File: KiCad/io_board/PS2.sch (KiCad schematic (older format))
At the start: 1 part

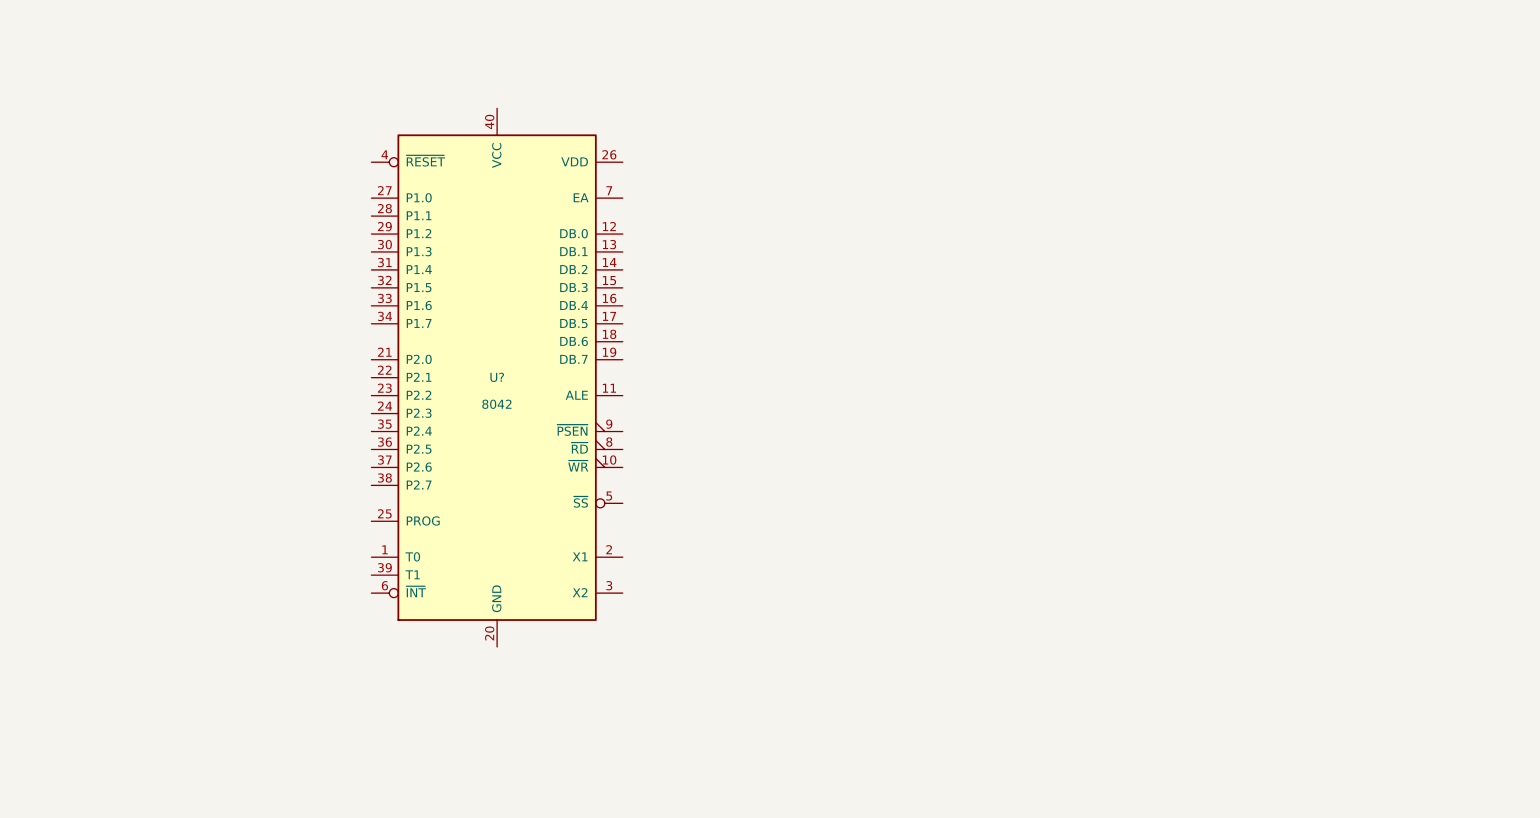
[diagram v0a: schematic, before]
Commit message: Updated IO board schematics and board.
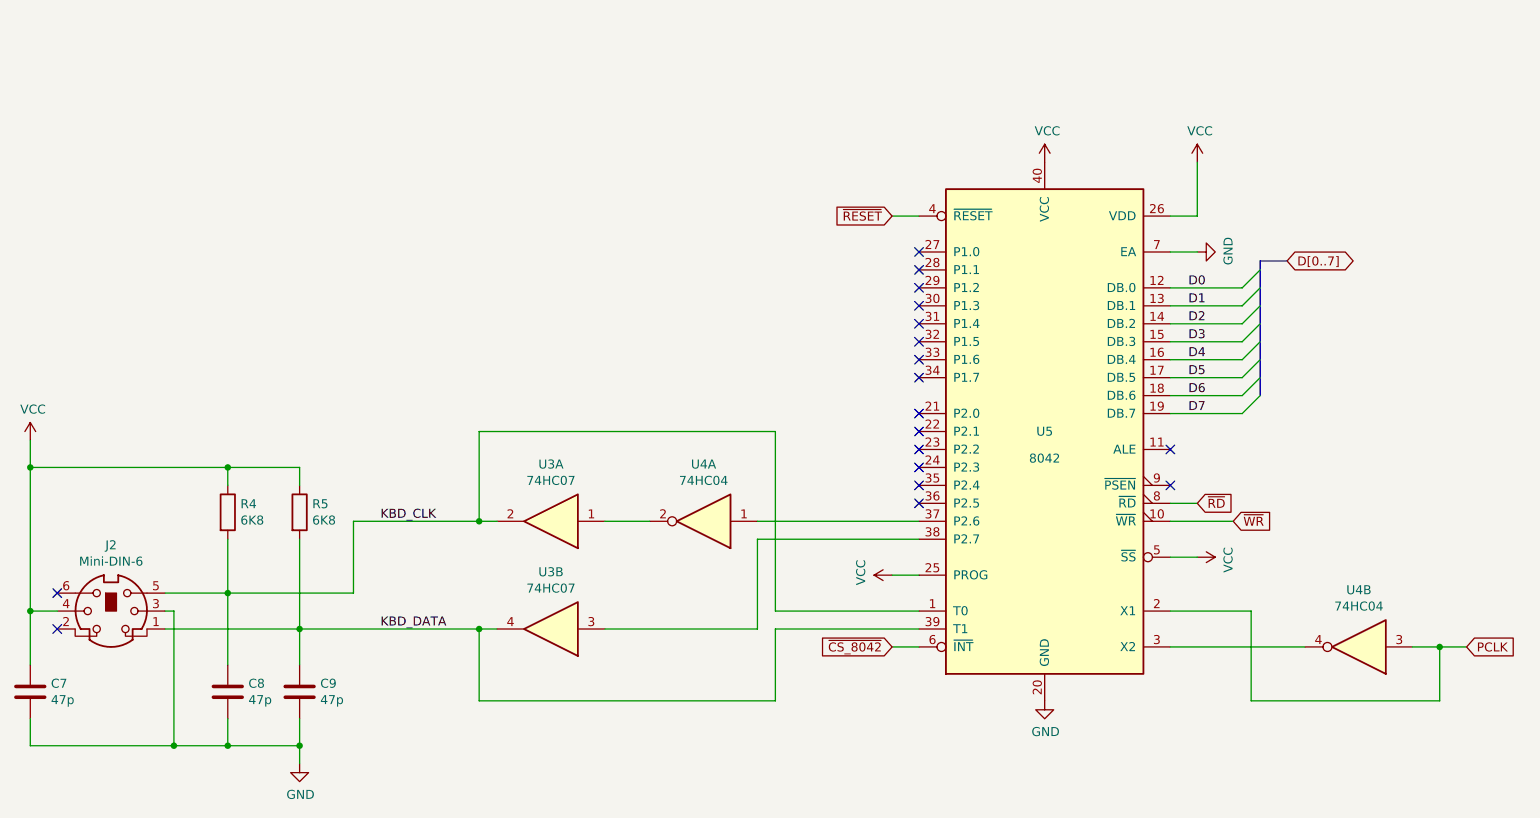
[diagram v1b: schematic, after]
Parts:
- added C7, C8, C9: 47p, Capacitor_THT:C_Disc_D3.0mm_W1.6mm_P2.50mm, symbol Device:C
- added J2: Mini-DIN-6, Mini8086:Mini_din6, symbol Connector:Mini-DIN-6
- added R4, R5: 6K8, Resistor_THT:R_Axial_DIN0207_L6.3mm_D2.5mm_P7.62mm_Horizontal, symbol Device:R
- added U3: 74HC07, Package_DIP:DIP-14_W7.62mm_LongPads, symbol 74xx:SN74LS07N
- added U4: 74HC04, symbol 74xx:74HC04
- U5: renamed from U?; footprint (none) -> Package_DIP:DIP-40_W15.24mm_Socket_LongPads
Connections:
- net KBD_CLK: now reaches U5.1 (T0)
- net KBD_CLK: now also C8.1, J2.5, R4.2, U3.2
- net ~WR: now reaches U5.10 (~WR~)
- net D0: now reaches U5.12 (DB.0)
- net D1: now reaches U5.13 (DB.1)
- net D2: now reaches U5.14 (DB.2)
- net D3: now reaches U5.15 (DB.3)
- net D4: now reaches U5.16 (DB.4)
- net D5: now reaches U5.17 (DB.5)
- net D6: now reaches U5.18 (DB.6)
- net D7: now reaches U5.19 (DB.7)
- net PCLK: now reaches U5.2 (X1)
- net PCLK: now also U4.3
- net GND: now reaches U5.20 (GND)
- net GND: now also U5.7 (EA), C7.2, C8.2, C9.2, J2.3
- net VCC: now reaches U5.25 (PROG)
- net VCC: now also U5.26 (VDD), U5.40 (VCC), U5.5 (~SS~), C7.1, J2.4, R4.1, R5.1
- net at U5.3 (X2): now also U4.4
- net at U5.37 (P2.6): now also U4.1
- net at U5.38 (P2.7): now also U3.3
- net KBD_DATA: now reaches U5.39 (T1)
- net KBD_DATA: now also C9.1, J2.1, R5.2, U3.4
- net ~RESET: now reaches U5.4 (~RESET~)
- net ~CS_8042: now reaches U5.6 (~INT~)
- net ~RD: now reaches U5.8 (~RD~)
- new net: U3.1, U4.2
- no-connect marks 0 -> 18
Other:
- moved on the sheet: U5

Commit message: Worked on I/O board.
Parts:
- U4: footprint (none) -> Package_SO:SOIC-14_3.9x8.7mm_P1.27mm
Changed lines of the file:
@@
 encoding utf-8
 Sheet 3 7
-Title ""
-Date ""
+Title "Mini8086 I/O board"
+Date "2020-11-05"
 Rev "1.0"
 Comp ""
@@
 F 0 "U4" H 5550 3533 50  0000 C CNN
 F 1 "74HC04" H 5550 3624 50  0000 C CNN
-F 2 "" H 5550 3850 50  0001 C CNN
+F 2 "Package_SO:SOIC-14_3.9x8.7mm_P1.27mm" H 5550 3850 50  0001 C CNN
 F 3 "https://assets.nexperia.com/documents/data-sheet/74HC_HCT04.pdf" H 5550 3850 50  0001 C CNN
 	1    5550 3850
@@
 F 0 "U4" H 9200 4233 50  0000 C CNN
 F 1 "74HC04" H 9200 4324 50  0000 C CNN
-F 2 "" H 9200 4550 50  0001 C CNN
+F 2 "Package_SO:SOIC-14_3.9x8.7mm_P1.27mm" H 9200 4550 50  0001 C CNN
 F 3 "https://assets.nexperia.com/documents/data-sheet/74HC_HCT04.pdf" H 9200 4550 50  0001 C CNN
 	2    9200 4550

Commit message: Working on IO board
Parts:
- added unit 7 of U3
- U4: value 74HC04 -> 74HCT04
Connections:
- net GND: now also U3.7 (GND)
- net VCC: now also U3.14 (VCC)
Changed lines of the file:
@@
 $Descr A4 11693 8268
 encoding utf-8
-Sheet 3 7
+Sheet 3 8
 Title "Mini8086 I/O board"
 Date "2020-11-05"
@@
 P 5550 3850
 F 0 "U4" H 5550 3533 50  0000 C CNN
-F 1 "74HC04" H 5550 3624 50  0000 C CNN
+F 1 "74HCT04" H 5550 3624 50  0000 C CNN
 F 2 "Package_SO:SOIC-14_3.9x8.7mm_P1.27mm" H 5550 3850 50  0001 C CNN
 F 3 "https://assets.nexperia.com/documents/data-sheet/74HC_HCT04.pdf" H 5550 3850 50  0001 C CNN
@@
 P 9200 4550
 F 0 "U4" H 9200 4233 50  0000 C CNN
-F 1 "74HC04" H 9200 4324 50  0000 C CNN
+F 1 "74HCT04" H 9200 4324 50  0000 C CNN
 F 2 "Package_SO:SOIC-14_3.9x8.7mm_P1.27mm" H 9200 4550 50  0001 C CNN
 F 3 "https://assets.nexperia.com/documents/data-sheet/74HC_HCT04.pdf" H 9200 4550 50  0001 C CNN
@@
 	-1   0    0    1
 $EndComp
+$Comp
+L 74xx:SN74LS07N U3
+U 7 1 5FABB725
+P 3400 2200
+F 0 "U3" H 3630 2246 50  0000 L CNN
+F 1 "74HC07" H 3630 2155 50  0000 L CNN
+F 2 "Package_DIP:DIP-14_W7.62mm_LongPads" H 3400 2200 50  0001 C CNN
+F 3 "www.ti.com/lit/ds/symlink/sn74ls07.pdf" H 3400 2200 50  0001 C CNN
+	7    3400 2200
+	1    0    0    -1
+$EndComp
+$Comp
+L power:GND #PWR041
+U 1 1 5FABDAD2
+P 3400 2700
+F 0 "#PWR041" H 3400 2450 50  0001 C CNN
+F 1 "GND" H 3405 2527 50  0000 C CNN
+F 2 "" H 3400 2700 50  0001 C CNN
+F 3 "" H 3400 2700 50  0001 C CNN
+	1    3400 2700
+	1    0    0    -1
+$EndComp
+$Comp
+L power:VCC #PWR031
+U 1 1 5FABE199
+P 3400 1700
+F 0 "#PWR031" H 3400 1550 50  0001 C CNN
+F 1 "VCC" H 3415 1873 50  0000 C CNN
+F 2 "" H 3400 1700 50  0001 C CNN
+F 3 "" H 3400 1700 50  0001 C CNN
+	1    3400 1700
+	1    0    0    -1
+$EndComp
 Wire Bus Line

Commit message: Worked on I/O board.
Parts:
- R4, R5: footprint Resistor_THT:R_Axial_DIN0207_L6.3mm_D2.5mm_P7.62mm_Horizontal -> Resistor_THT:R_Axial_DIN0207_L6.3mm_D2.5mm_P2.54mm_Vertical
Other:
- moved on the sheet: U3G
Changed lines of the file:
@@
 F 0 "R4" H 2970 3846 50  0000 L CNN
 F 1 "6K8" H 2970 3755 50  0000 L CNN
-F 2 "Resistor_THT:R_Axial_DIN0207_L6.3mm_D2.5mm_P7.62mm_Horizontal" V 2830 3800 50  0001 C CNN
+F 2 "Resistor_THT:R_Axial_DIN0207_L6.3mm_D2.5mm_P2.54mm_Vertical" V 2830 3800 50  0001 C CNN
 F 3 "~" H 2900 3800 50  0001 C CNN
 	1    2900 3800
@@
 F 0 "R5" H 3370 3846 50  0000 L CNN
 F 1 "6K8" H 3370 3755 50  0000 L CNN
-F 2 "Resistor_THT:R_Axial_DIN0207_L6.3mm_D2.5mm_P7.62mm_Horizontal" V 3230 3800 50  0001 C CNN
+F 2 "Resistor_THT:R_Axial_DIN0207_L6.3mm_D2.5mm_P2.54mm_Vertical" V 3230 3800 50  0001 C CNN
 F 3 "~" H 3300 3800 50  0001 C CNN
 	1    3300 3800
@@
 L 74xx:SN74LS07N U3
 U 7 1 5FABB725
-P 3400 2200
-F 0 "U3" H 3630 2246 50  0000 L CNN
-F 1 "74HC07" H 3630 2155 50  0000 L CNN
-F 2 "Package_DIP:DIP-14_W7.62mm_LongPads" H 3400 2200 50  0001 C CNN
-F 3 "www.ti.com/lit/ds/symlink/sn74ls07.pdf" H 3400 2200 50  0001 C CNN
-	7    3400 2200
+P 2600 1750
+F 0 "U3" H 2830 1796 50  0000 L CNN
+F 1 "74HC07" H 2830 1705 50  0000 L CNN
+F 2 "Package_DIP:DIP-14_W7.62mm_LongPads" H 2600 1750 50  0001 C CNN
+F 3 "www.ti.com/lit/ds/symlink/sn74ls07.pdf" H 2600 1750 50  0001 C CNN
+	7    2600 1750
 	1    0    0    -1
 $EndComp
@@
 L power:GND #PWR041
 U 1 1 5FABDAD2
-P 3400 2700
-F 0 "#PWR041" H 3400 2450 50  0001 C CNN
-F 1 "GND" H 3405 2527 50  0000 C CNN
-F 2 "" H 3400 2700 50  0001 C CNN
-F 3 "" H 3400 2700 50  0001 C CNN
-	1    3400 2700
+P 2600 2250
+F 0 "#PWR041" H 2600 2000 50  0001 C CNN
+F 1 "GND" H 2605 2077 50  0000 C CNN
+F 2 "" H 2600 2250 50  0001 C CNN
+F 3 "" H 2600 2250 50  0001 C CNN
+	1    2600 2250
 	1    0    0    -1
 $EndComp
@@
 L power:VCC #PWR031
 U 1 1 5FABE199
-P 3400 1700
-F 0 "#PWR031" H 3400 1550 50  0001 C CNN
-F 1 "VCC" H 3415 1873 50  0000 C CNN
-F 2 "" H 3400 1700 50  0001 C CNN
-F 3 "" H 3400 1700 50  0001 C CNN
-	1    3400 1700
+P 2600 1250
+F 0 "#PWR031" H 2600 1100 50  0001 C CNN
+F 1 "VCC" H 2615 1423 50  0000 C CNN
+F 2 "" H 2600 1250 50  0001 C CNN
+F 3 "" H 2600 1250 50  0001 C CNN
+	1    2600 1250
 	1    0    0    -1
 $EndComp

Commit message: Continued work on I/O board.
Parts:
- C7, C8, C9: footprint Capacitor_THT:C_Disc_D3.0mm_W1.6mm_P2.50mm -> Capacitor_SMD:C_1206_3216Metric
- R4, R5: footprint Resistor_THT:R_Axial_DIN0207_L6.3mm_D2.5mm_P2.54mm_Vertical -> Resistor_SMD:R_1206_3216Metric
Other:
- moved on the sheet: U3G
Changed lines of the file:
@@
 F 0 "C9" H 3415 4846 50  0000 L CNN
 F 1 "47p" H 3415 4755 50  0000 L CNN
-F 2 "Capacitor_THT:C_Disc_D3.0mm_W1.6mm_P2.50mm" H 3338 4650 50  0001 C CNN
+F 2 "Capacitor_SMD:C_1206_3216Metric" H 3338 4650 50  0001 C CNN
 F 3 "~" H 3300 4800 50  0001 C CNN
 	1    3300 4800
@@
 F 0 "C8" H 3015 4846 50  0000 L CNN
 F 1 "47p" H 3015 4755 50  0000 L CNN
-F 2 "Capacitor_THT:C_Disc_D3.0mm_W1.6mm_P2.50mm" H 2938 4650 50  0001 C CNN
+F 2 "Capacitor_SMD:C_1206_3216Metric" H 2938 4650 50  0001 C CNN
 F 3 "~" H 2900 4800 50  0001 C CNN
 	1    2900 4800
@@
 F 0 "C7" H 1915 4846 50  0000 L CNN
 F 1 "47p" H 1915 4755 50  0000 L CNN
-F 2 "Capacitor_THT:C_Disc_D3.0mm_W1.6mm_P2.50mm" H 1838 4650 50  0001 C CNN
+F 2 "Capacitor_SMD:C_1206_3216Metric" H 1838 4650 50  0001 C CNN
 F 3 "~" H 1800 4800 50  0001 C CNN
 	1    1800 4800
@@
 F 0 "R4" H 2970 3846 50  0000 L CNN
 F 1 "6K8" H 2970 3755 50  0000 L CNN
-F 2 "Resistor_THT:R_Axial_DIN0207_L6.3mm_D2.5mm_P2.54mm_Vertical" V 2830 3800 50  0001 C CNN
+F 2 "Resistor_SMD:R_1206_3216Metric" V 2830 3800 50  0001 C CNN
 F 3 "~" H 2900 3800 50  0001 C CNN
 	1    2900 3800
@@
 F 0 "R5" H 3370 3846 50  0000 L CNN
 F 1 "6K8" H 3370 3755 50  0000 L CNN
-F 2 "Resistor_THT:R_Axial_DIN0207_L6.3mm_D2.5mm_P2.54mm_Vertical" V 3230 3800 50  0001 C CNN
+F 2 "Resistor_SMD:R_1206_3216Metric" V 3230 3800 50  0001 C CNN
 F 3 "~" H 3300 3800 50  0001 C CNN
 	1    3300 3800
@@
 L 74xx:SN74LS07N U3
 U 7 1 5FABB725
-P 2600 1750
-F 0 "U3" H 2830 1796 50  0000 L CNN
-F 1 "74HC07" H 2830 1705 50  0000 L CNN
-F 2 "Package_DIP:DIP-14_W7.62mm_LongPads" H 2600 1750 50  0001 C CNN
-F 3 "www.ti.com/lit/ds/symlink/sn74ls07.pdf" H 2600 1750 50  0001 C CNN
-	7    2600 1750
+P 2200 1800
+F 0 "U3" H 2430 1846 50  0000 L CNN
+F 1 "74HC07" H 2430 1755 50  0000 L CNN
+F 2 "Package_DIP:DIP-14_W7.62mm_LongPads" H 2200 1800 50  0001 C CNN
+F 3 "www.ti.com/lit/ds/symlink/sn74ls07.pdf" H 2200 1800 50  0001 C CNN
+	7    2200 1800
 	1    0    0    -1
 $EndComp
@@
 L power:GND #PWR041
 U 1 1 5FABDAD2
-P 2600 2250
-F 0 "#PWR041" H 2600 2000 50  0001 C CNN
-F 1 "GND" H 2605 2077 50  0000 C CNN
-F 2 "" H 2600 2250 50  0001 C CNN
-F 3 "" H 2600 2250 50  0001 C CNN
-	1    2600 2250
+P 2200 2300
+F 0 "#PWR041" H 2200 2050 50  0001 C CNN
+F 1 "GND" H 2205 2127 50  0000 C CNN
+F 2 "" H 2200 2300 50  0001 C CNN
+F 3 "" H 2200 2300 50  0001 C CNN
+	1    2200 2300
 	1    0    0    -1
 $EndComp
@@
 L power:VCC #PWR031
 U 1 1 5FABE199
-P 2600 1250
-F 0 "#PWR031" H 2600 1100 50  0001 C CNN
-F 1 "VCC" H 2615 1423 50  0000 C CNN
-F 2 "" H 2600 1250 50  0001 C CNN
-F 3 "" H 2600 1250 50  0001 C CNN
-	1    2600 1250
+P 2200 1300
+F 0 "#PWR031" H 2200 1150 50  0001 C CNN
+F 1 "VCC" H 2215 1473 50  0000 C CNN
+F 2 "" H 2200 1300 50  0001 C CNN
+F 3 "" H 2200 1300 50  0001 C CNN
+	1    2200 1300
 	1    0    0    -1
 $EndComp

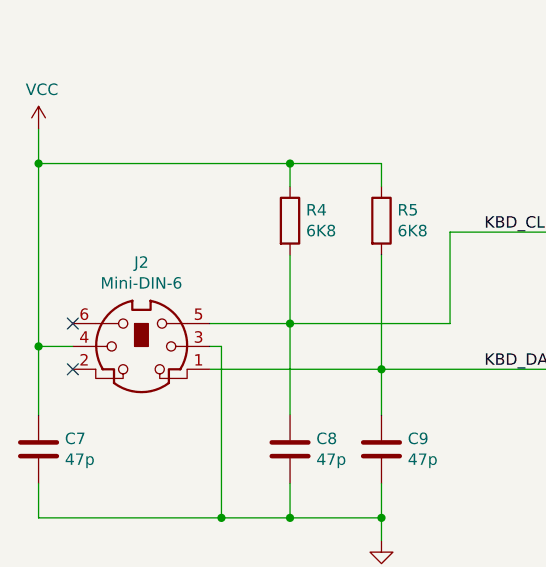
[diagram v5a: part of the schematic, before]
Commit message: Updated I/O board.
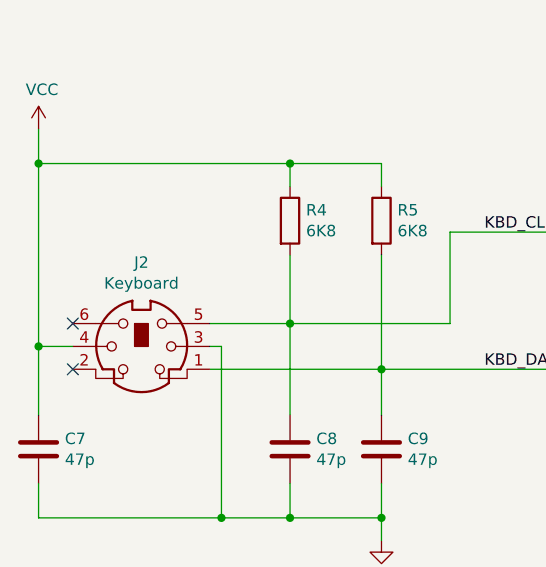
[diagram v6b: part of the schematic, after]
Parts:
- J2: value Mini-DIN-6 -> Keyboard
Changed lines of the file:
@@
 P 2250 4350
 F 0 "J2" H 2250 4717 50  0000 C CNN
-F 1 "Mini-DIN-6" H 2250 4626 50  0000 C CNN
+F 1 "Keyboard" H 2250 4626 50  0000 C CNN
 F 2 "Mini8086:Mini_din6" H 2250 4350 50  0001 C CNN
 F 3 "http://service.powerdynamics.com/ec/Catalog17/Section%2011.pdf" H 2250 4350 50  0001 C CNN

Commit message: Updated I/O board
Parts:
- U3: footprint Package_DIP:DIP-14_W7.62mm_LongPads -> Package_SO:SOIC-14_3.9x8.7mm_P1.27mm
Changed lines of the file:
@@
 F 0 "U3" H 4700 4133 50  0000 C CNN
 F 1 "74HC07" H 4700 4224 50  0000 C CNN
-F 2 "Package_DIP:DIP-14_W7.62mm_LongPads" H 4700 4450 50  0001 C CNN
+F 2 "Package_SO:SOIC-14_3.9x8.7mm_P1.27mm" H 4700 4450 50  0001 C CNN
 F 3 "www.ti.com/lit/ds/symlink/sn74ls07.pdf" H 4700 4450 50  0001 C CNN
 	2    4700 4450
@@
 F 0 "U3" H 4700 3533 50  0000 C CNN
 F 1 "74HC07" H 4700 3624 50  0000 C CNN
-F 2 "Package_DIP:DIP-14_W7.62mm_LongPads" H 4700 3850 50  0001 C CNN
+F 2 "Package_SO:SOIC-14_3.9x8.7mm_P1.27mm" H 4700 3850 50  0001 C CNN
 F 3 "www.ti.com/lit/ds/symlink/sn74ls07.pdf" H 4700 3850 50  0001 C CNN
 	1    4700 3850
@@
 F 0 "U3" H 2430 1846 50  0000 L CNN
 F 1 "74HC07" H 2430 1755 50  0000 L CNN
-F 2 "Package_DIP:DIP-14_W7.62mm_LongPads" H 2200 1800 50  0001 C CNN
+F 2 "Package_SO:SOIC-14_3.9x8.7mm_P1.27mm" H 2200 1800 50  0001 C CNN
 F 3 "www.ti.com/lit/ds/symlink/sn74ls07.pdf" H 2200 1800 50  0001 C CNN
 	7    2200 1800

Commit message: Worked on I/O board.
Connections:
- net IRQ1: now reaches U5.35 (P2.4)
- net A0: now reaches U5.9 (~PSEN~)
- no-connect marks 18 -> 16
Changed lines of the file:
@@
 NoConn ~ 6750 3550
 NoConn ~ 6750 3450
-NoConn ~ 6750 3650
 NoConn ~ 6750 3350
 NoConn ~ 6750 3250
@@
 	1    0    0    -1
 $EndComp
-NoConn ~ 8150 3650
 $Comp
 L Device:R R4
@@
 	1    0    0    -1
 $EndComp
+Wire Wire Line
+	8150 3650 8500 3650
+Wire Wire Line
+	6750 3650 6600 3650
+Text GLabel 6600 3650 0    50   Output ~ 0
+IRQ1
+Entry Wire Line
+	8500 3650 8600 3550
+Wire Bus Line
+	8600 3550 8600 3450
+Wire Bus Line
+	8600 3450 8700 3450
 Wire Bus Line
 	8650 2400 8650 3150
+Text GLabel 8700 3450 2    50   Input ~ 0
+A[0..19]
+Text Label 8300 3650 0    50   ~ 0
+A0
 $EndSCHEMATC
